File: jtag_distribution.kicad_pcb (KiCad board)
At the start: 2 copper layers, 150 x 50 mm, 45 parts, among them J1 Conn_01x06, J10 Conn_01x06, J11 Conn_01x06, J12 Conn_01x06, J13 Conn_01x06, J14 Conn_01x06, J15 Conn_01x06, J16 Conn_ARM_JTAG_SWD_20, J2 Conn_01x06, J3 Conn_01x06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

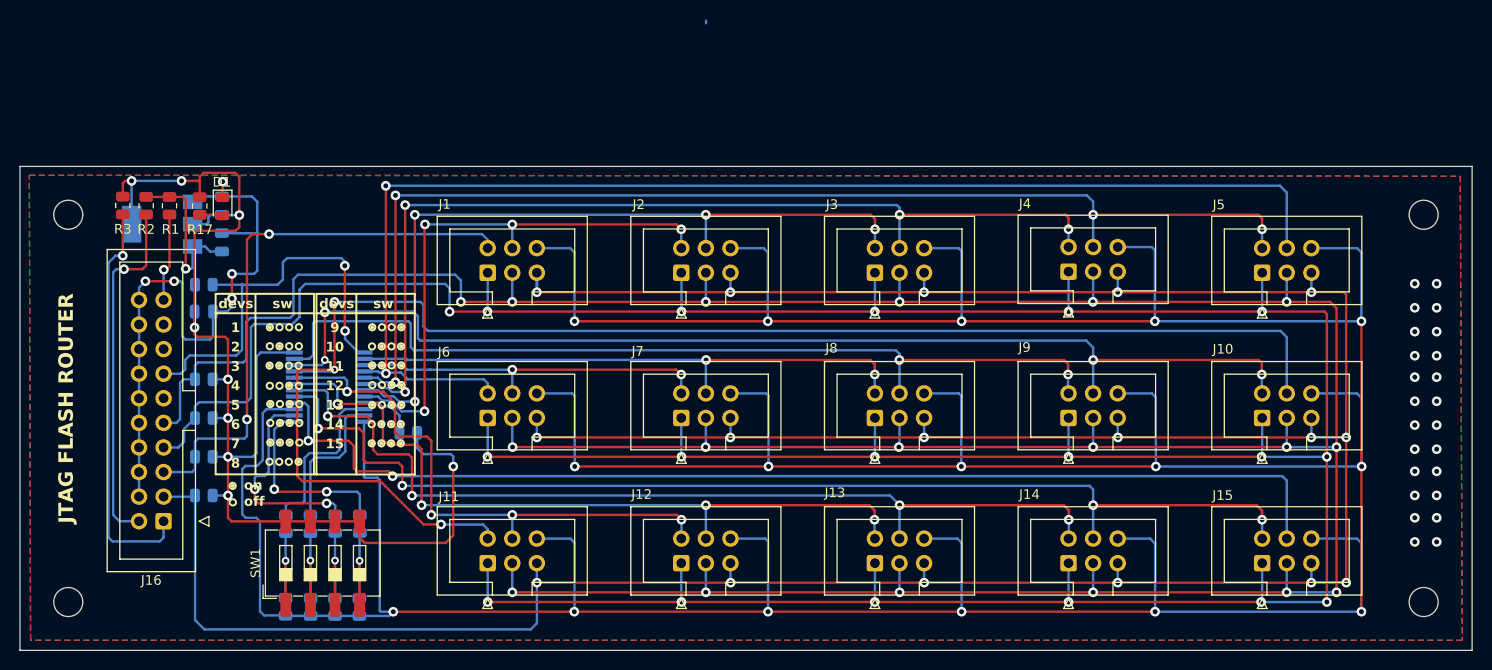
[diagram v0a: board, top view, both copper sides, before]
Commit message: change dip switch type, change reset position
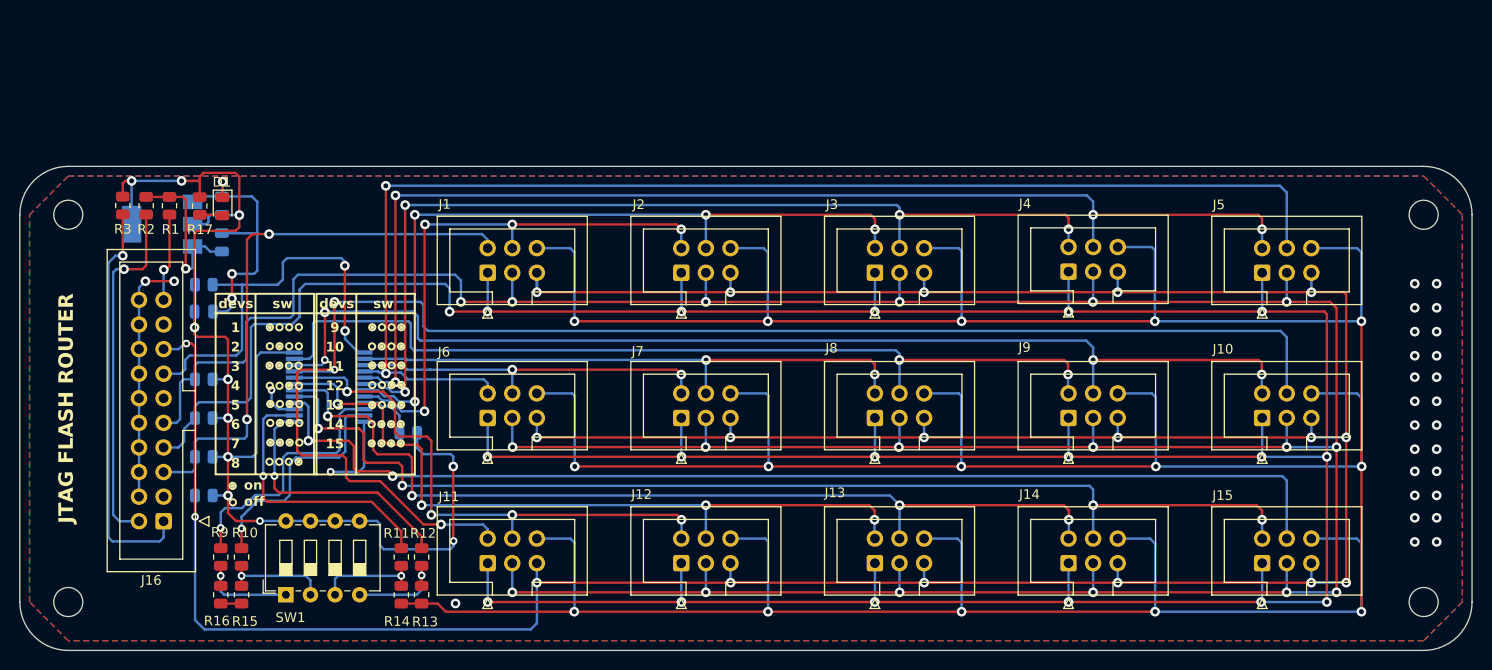
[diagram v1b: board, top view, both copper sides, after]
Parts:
- R10, R11, R12, R13, R14, R15, R16, R9: moved to F.Cu
- SW1: footprint Button_Switch_SMD:SW_DIP_SPSTx04_Slide_6.7x11.72mm_W8.61mm_P2.54mm_LowProfile -> Button_Switch_THT:SW_DIP_SPSTx04_Slide_6.7x11.72mm_W7.62mm_P2.54mm_LowProfile
- moved R10 7.88 mm to (42.9, 80.3)
- moved R11 7.63 mm to (59.4, 80.3)
- moved R9 7.53 mm to (40.8, 80.3)
- moved R15 7.25 mm to (42.9, 84.2)
- moved R12 7.24 mm to (61.5, 80.3)
- moved R14 6.96 mm to (59.4, 84.2)
- moved R16 6.81 mm to (40.8, 84.2)
- moved R13 6.56 mm to (61.5, 84.2)
- moved SW1 5.02 mm to (47.5, 84.2)
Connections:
- J1 pad 5: /distribution/TRST -> /distribution/RST
- J10 pad 5: /distribution/TRST -> /distribution/RST
- J11 pad 5: /distribution/TRST -> /distribution/RST
- J12 pad 5: /distribution/TRST -> /distribution/RST
- J13 pad 5: /distribution/TRST -> /distribution/RST
- J14 pad 5: /distribution/TRST -> /distribution/RST
- J15 pad 5: /distribution/TRST -> /distribution/RST
- J16 pad 15: unconnected-(J16-~{SRST}-Pad15) -> /distribution/RST
- J16 pad 3: /distribution/TRST -> unconnected-(J16-~{TRST}-Pad3)
- J2 pad 5: /distribution/TRST -> /distribution/RST
- J3 pad 5: /distribution/TRST -> /distribution/RST
- J4 pad 5: /distribution/TRST -> /distribution/RST
- J5 pad 5: /distribution/TRST -> /distribution/RST
- J6 pad 5: /distribution/TRST -> /distribution/RST
- J7 pad 5: /distribution/TRST -> /distribution/RST
- J8 pad 5: /distribution/TRST -> /distribution/RST
- J9 pad 5: /distribution/TRST -> /distribution/RST
- R8 pad 1: /distribution/TRST -> /distribution/RST
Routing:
- net /distribution/RST: track 0.00 -> 385.3 mm, vias 0 -> 19
- net /distribution/TRST: track 367.3 -> 0.00 mm, vias 17 -> 0
- net GND: track 593.2 -> 531.2 mm, vias 45 -> 47
- net /SW1: track 15.2 -> 24.3 mm, vias 0 -> 1
- net /SW0: track 18.0 -> 27.1 mm, vias 0 -> 1
- net /SW2: track 21.6 -> 29.1 mm, vias 2 -> 1
- net /SW3: track 19.8 -> 27.0 mm, vias 2 -> 1
- net Net-(R12-Pad2): track 11.3 -> 10.2 mm
- net Net-(R16-Pad2): track 11.3 -> 10.5 mm
- net Net-(R11-Pad2): track 11.3 -> 10.7 mm
- net +3V3: track 135.7 -> 135.9 mm, vias 9 -> 11
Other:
- outline, holes or cut-outs redrawn
